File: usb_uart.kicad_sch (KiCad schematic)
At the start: 6 parts, among them U3 FT230XS

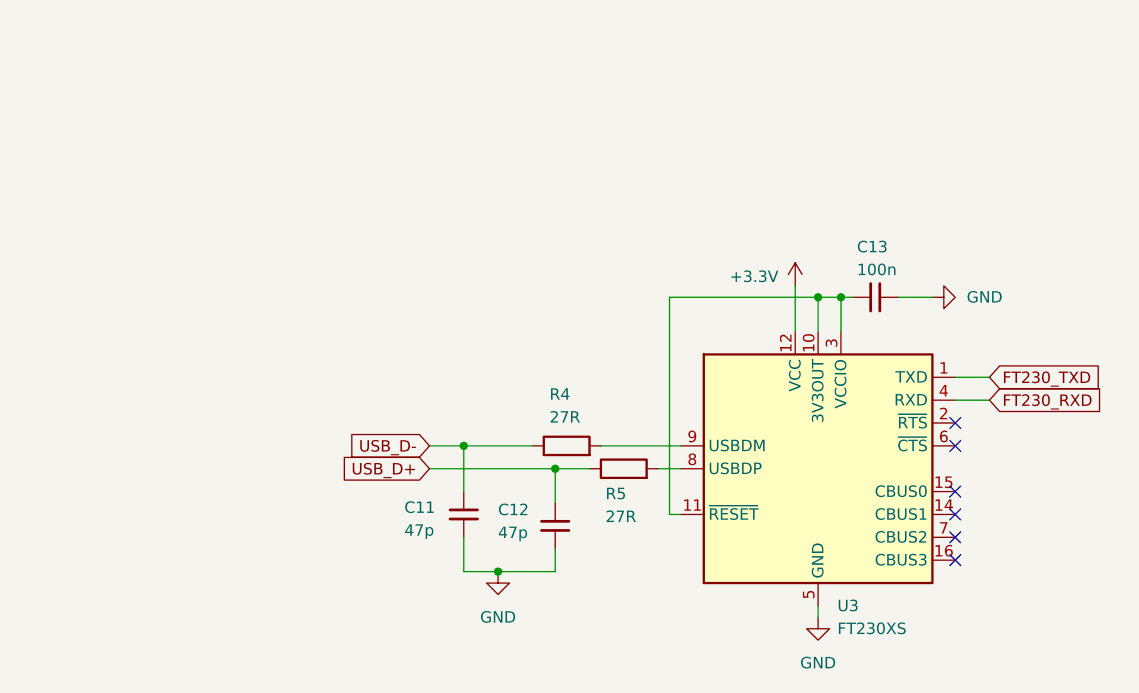
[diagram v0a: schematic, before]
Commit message: [usb-uart] Connects VCC with 3V3OUT and VCCIO
This needs to be done because FT230X is provided with 3.3V, if 3.3V is
provided, as per the datasheet, 3V3OUT becomes an input and requires
3.3V input. VCCIO now also needs to be fed with the same 3.3V as per the
schematic. Although, in the schematic, VCC is not directly connected,
but that is because in the RS485 application schematic, VCC is driven by
5V and not 3.3V.
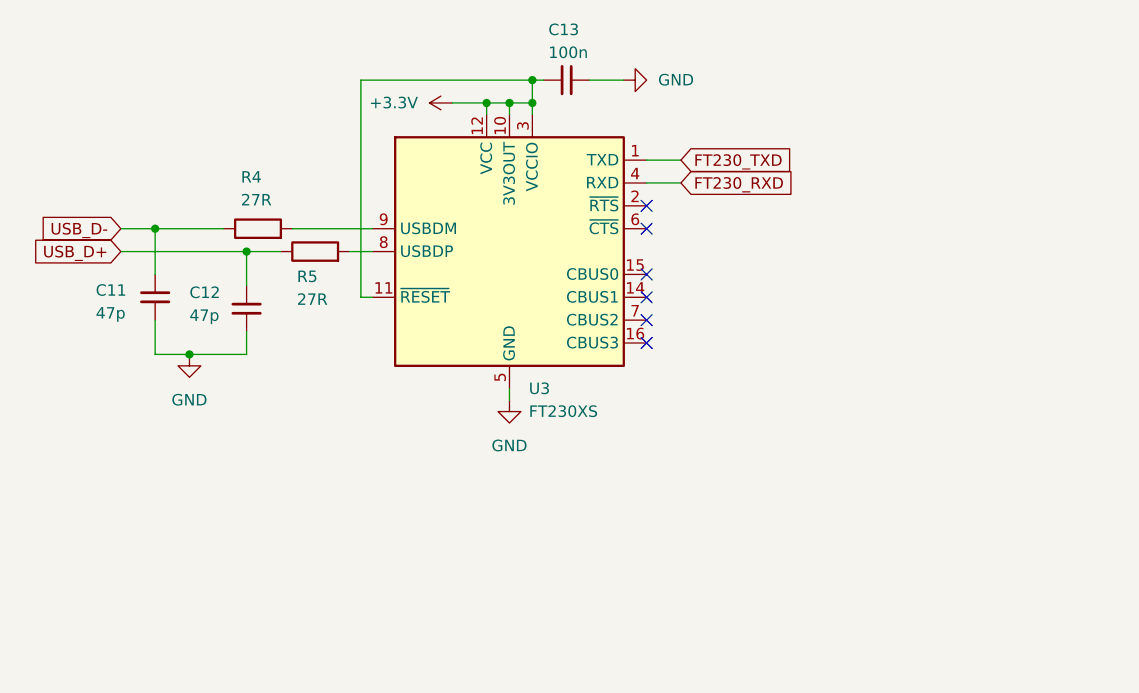
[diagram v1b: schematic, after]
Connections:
- net +3.3V: now also C13.2, U3.10 (3V3OUT), U3.11 (~{RESET}), U3.3 (VCCIO)

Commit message: [refactor] Refactor the schematics to use sub-sheets
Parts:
- removed C11, C12: 47p, symbol Device:C_Small
- removed C13: 100n, symbol Device:C_Small
- removed R4, R5: 27R, symbol Device:R
- removed U3: FT230XS, Package_SO:SSOP-16_3.9x4.9mm_P0.635mm, symbol Interface_USB:FT230XS
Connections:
- no-connect marks 6 -> 0
